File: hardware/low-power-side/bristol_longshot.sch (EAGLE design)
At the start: 83 parts, among them Q1 NX2301P, U1 SAM_D20E, U10 ADP1607ACPZN-R7, U11 TPS73118DBVT, U12 74LVC1G04GW, U14 SIT1552, U16 SIT1552, U2 SI4461, U3 SE880, U4 SST25WF040BT-40I/NP, U5 TG-5006CJ, U6 TG-5006CJ, U7 ADM6823WYRJZ, U8 SN74LVC1G32DCKR, U9 MS5607-02BA03

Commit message: [low-power] |v0.987.2|Low Power. Adjusted 100µF cap from 1210 to 1206
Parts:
- C32: device resistor:C-EUC1210K -> resistor:C-EUC1206K
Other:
- note added: "Icc = 10µA max"
- note added: "Icc = 5µA nominal at 1.8V"
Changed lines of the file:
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@@
 <part name="U$34" library="microbuilder_v3" deviceset="GND" device=""/>
 <part name="U$36" library="microbuilder_v3" deviceset="GND" device=""/>
-<part name="C32" library="resistor" deviceset="C-EU" device="C1210K" value="100µF"/>
-<part name="U$32" library="microbuilder_v3" deviceset="GND" device=""/>
 <part name="C10" library="microbuilder_v3" deviceset="CAP_CERAMIC" device="_0402" value="100pF"/>
 <part name="R11" library="microbuilder_v3" deviceset="RESISTOR" device="_0402" value="100kΩ"/>
@@
 <part name="R16" library="microbuilder_v3" deviceset="RESISTOR" device="_0402" value="1MΩ"/>
 <part name="U$74" library="microbuilder_v3" deviceset="GND" device=""/>
+<part name="C32" library="resistor" deviceset="C-EU" device="C1206K" value="100µF"/>
+<part name="U$32" library="microbuilder_v3" deviceset="GND" device=""/>
 </parts>
 <sheets>
@@
 <text x="88.9" y="218.948" size="1.27" layer="97" font="vector" ratio="11" distance="100">t_WD is 0.93x nominal at -40ºC</text>
 <text x="162.56" y="165.608" size="1.27" layer="97" font="vector" ratio="11">XOSC32K_IN</text>
+<text x="93.98" y="191.008" size="1.27" layer="97" font="vector" ratio="11" distance="100">Icc = 5µA nominal at 1.8V</text>
+<text x="152.4" y="191.008" size="1.27" layer="97" font="vector" ratio="11" distance="100">Icc = 10µA max</text>
+<text x="469.9" y="61.468" size="1.27" layer="97" font="vector" ratio="11" distance="100">Icc = 10µA max</text>
 </plain>
 <instances>
@@
 <instance part="U$34" gate="G$1" x="464.82" y="182.88"/>
 <instance part="U$36" gate="G$1" x="454.66" y="182.88"/>
-<instance part="C32" gate="G$1" x="124.46" y="43.18"/>
-<instance part="U$32" gate="G$1" x="124.46" y="30.48"/>
 <instance part="C10" gate="G$1" x="297.18" y="48.26"/>
 <instance part="R11" gate="G$1" x="137.16" y="132.08" rot="R90"/>
@@
 <instance part="R16" gate="G$1" x="132.08" y="198.12" rot="R90"/>
 <instance part="U$74" gate="G$1" x="132.08" y="187.96"/>
+<instance part="C32" gate="G$1" x="124.46" y="43.18"/>
+<instance part="U$32" gate="G$1" x="124.46" y="30.48"/>
 </instances>
 <busses>
@@
 </segment>
 <segment>
-<pinref part="C32" gate="G$1" pin="2"/>
-<pinref part="U$32" gate="G$1" pin="GND"/>
-<wire x1="124.46" y1="38.1" x2="124.46" y2="33.02" width="0.1524" layer="91"/>
-</segment>
-<segment>
 <pinref part="R11" gate="G$1" pin="1"/>
 <pinref part="U$47" gate="G$1" pin="GND"/>
@@
 <pinref part="U$74" gate="G$1" pin="GND"/>
 <wire x1="132.08" y1="193.04" x2="132.08" y2="190.5" width="0.1524" layer="91"/>
+</segment>
+<segment>
+<pinref part="C32" gate="G$1" pin="2"/>
+<pinref part="U$32" gate="G$1" pin="GND"/>
+<wire x1="124.46" y1="33.02" x2="124.46" y2="38.1" width="0.1524" layer="91"/>
 </segment>
 </net>
@@
 <wire x1="101.6" y1="55.88" x2="111.76" y2="55.88" width="0.1524" layer="91"/>
 <junction x="111.76" y="55.88"/>
-<pinref part="C32" gate="G$1" pin="1"/>
 <wire x1="111.76" y1="55.88" x2="124.46" y2="55.88" width="0.1524" layer="91"/>
 <wire x1="124.46" y1="55.88" x2="124.46" y2="45.72" width="0.1524" layer="91"/>
-</segment>
-<segment>
+<pinref part="C32" gate="G$1" pin="1"/>
+</segment>
+<segment>

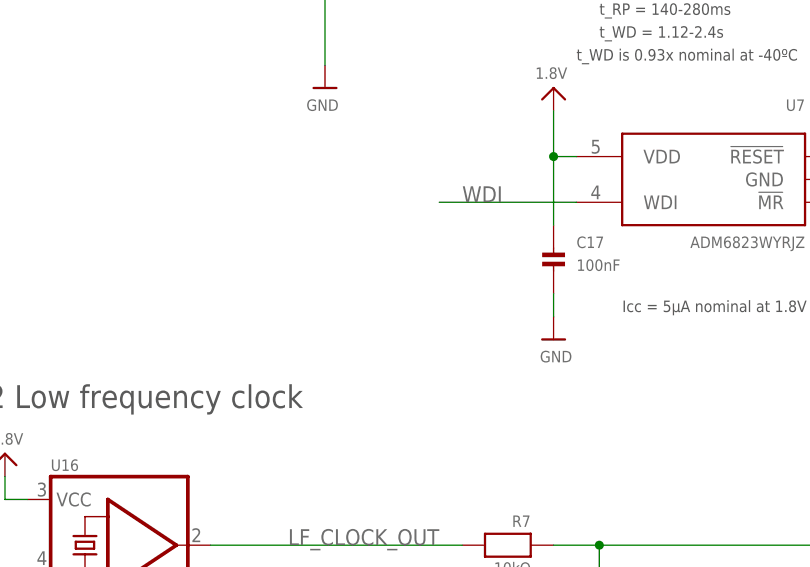
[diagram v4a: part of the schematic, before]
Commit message: [low-power] v0.987.3 Added pull-down on WDI
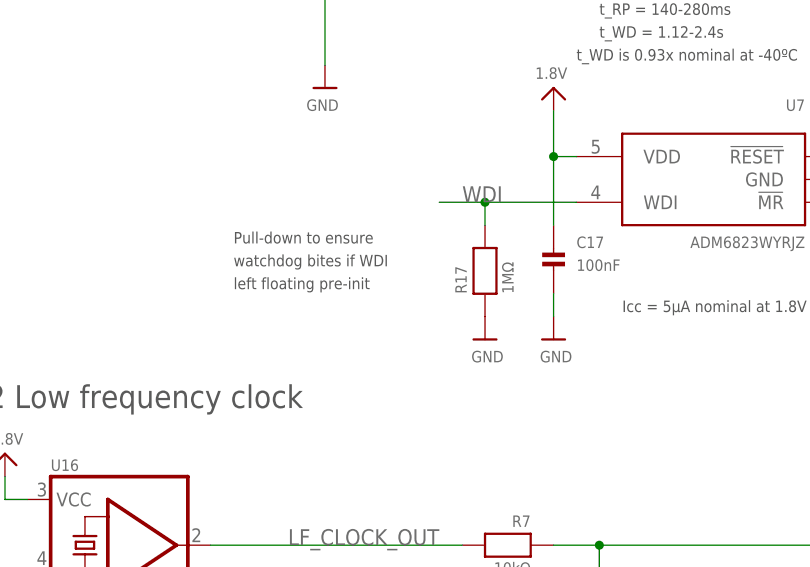
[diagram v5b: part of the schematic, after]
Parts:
- added R17: 1MΩ, microbuilder_v3:RESISTOR_0402
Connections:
- net GND: now also R17.1
- net WDI: now also R17.2
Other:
- note added: "Pull-down to ensure watchdog bites if WDI left floating pre-init"
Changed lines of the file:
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@@
 <part name="C32" library="resistor" deviceset="C-EU" device="C1206K" value="100µF"/>
 <part name="U$32" library="microbuilder_v3" deviceset="GND" device=""/>
+<part name="R17" library="microbuilder_v3" deviceset="RESISTOR" device="_0402" value="1MΩ"/>
+<part name="U$76" library="microbuilder_v3" deviceset="GND" device=""/>
 </parts>
 <sheets>
@@
 <text x="152.4" y="191.008" size="1.27" layer="97" font="vector" ratio="11" distance="100">Icc = 10µA max</text>
 <text x="469.9" y="61.468" size="1.27" layer="97" font="vector" ratio="11" distance="100">Icc = 10µA max</text>
+<text x="50.8" y="193.548" size="1.27" layer="97" font="vector" ratio="11" distance="100">Pull-down to ensure
+watchdog bites if WDI
+left floating pre-init</text>
 </plain>
 <instances>
@@
 <instance part="C32" gate="G$1" x="124.46" y="43.18"/>
 <instance part="U$32" gate="G$1" x="124.46" y="30.48"/>
+<instance part="R17" gate="G$1" x="78.74" y="195.58" rot="R90"/>
+<instance part="U$76" gate="G$1" x="78.74" y="187.96"/>
 </instances>
 <busses>
@@
 <pinref part="U$32" gate="G$1" pin="GND"/>
 <wire x1="124.46" y1="33.02" x2="124.46" y2="38.1" width="0.1524" layer="91"/>
+</segment>
+<segment>
+<pinref part="R17" gate="G$1" pin="1"/>
+<pinref part="U$76" gate="G$1" pin="GND"/>
 </segment>
 </net>
@@
 <segment>
 <pinref part="U7" gate="A" pin="WDI"/>
-<wire x1="88.9" y1="203.2" x2="73.66" y2="203.2" width="0.1524" layer="91"/>
+<wire x1="88.9" y1="203.2" x2="78.74" y2="203.2" width="0.1524" layer="91"/>
 <label x="76.2" y="203.2" size="1.778" layer="95"/>
-</segment>
-<segment>
+<pinref part="R17" gate="G$1" pin="2"/>
+<wire x1="78.74" y1="203.2" x2="73.66" y2="203.2" width="0.1524" layer="91"/>
+<wire x1="78.74" y1="203.2" x2="78.74" y2="200.66" width="0.1524" layer="91"/>
+<junction x="78.74" y="203.2"/>
+</segment>
+<segment>
